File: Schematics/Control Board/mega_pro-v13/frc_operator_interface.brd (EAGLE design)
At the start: 127 x 127 mm, 65 parts, among them J1 AVR_SPI_PRG_6PTH, U1 TLC59282_DBQ_24, U4 FT232RLSSOP, Y1 RESONATORSMD

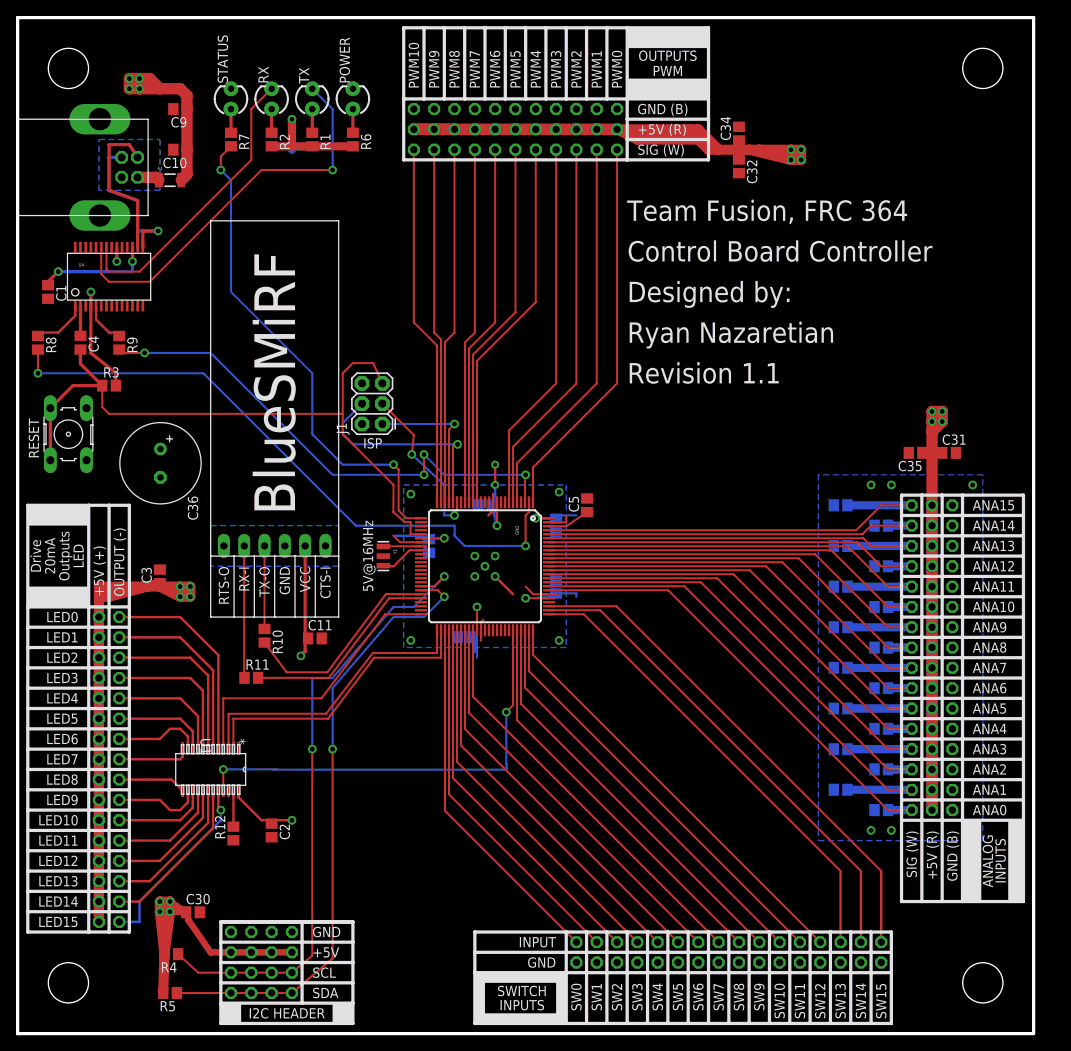
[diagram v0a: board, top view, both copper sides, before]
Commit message: Updated control board schematics and board layout
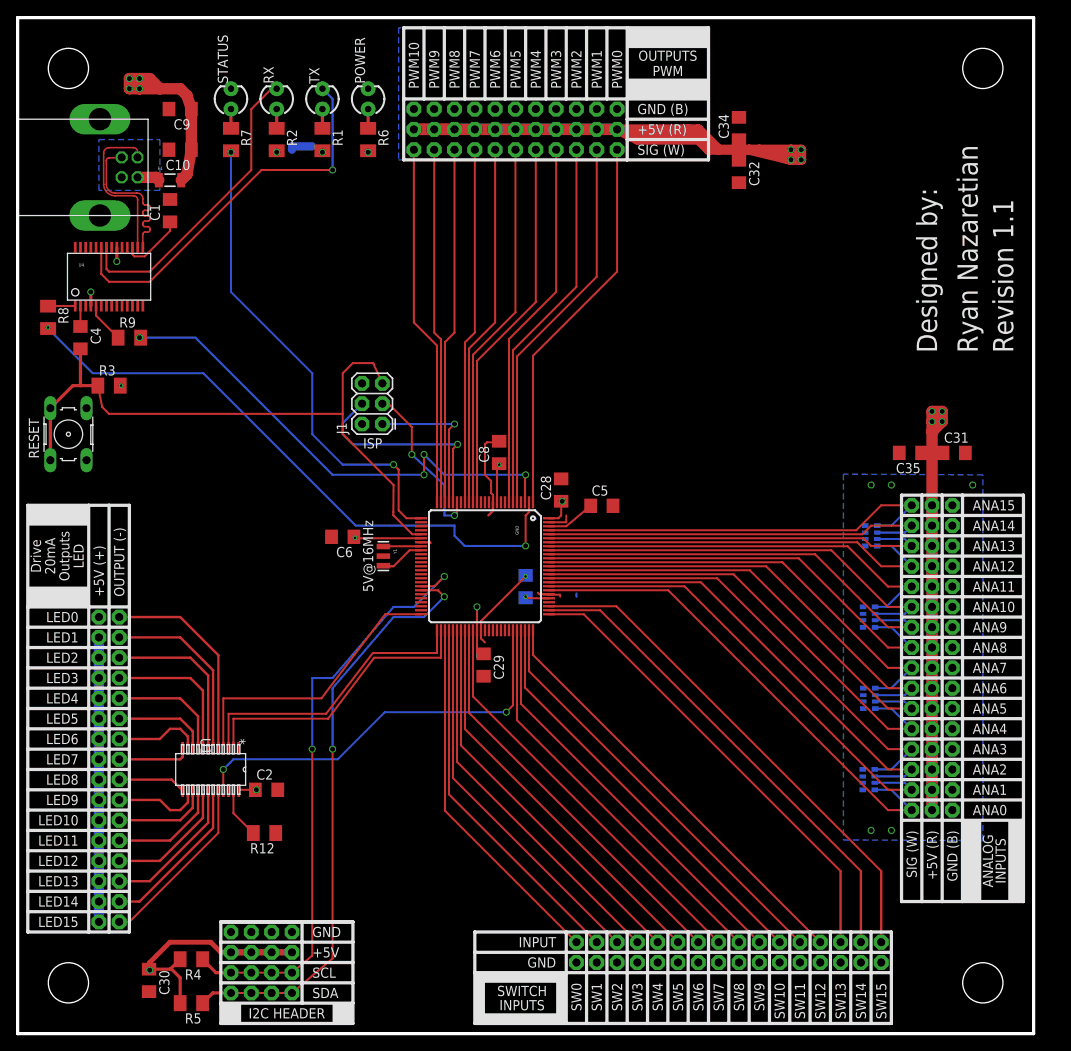
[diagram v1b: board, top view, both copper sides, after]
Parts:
- removed C11, C3: 10uF, resistor:C0805
- removed C12, C13, C14, C15, C16, C17, C18, C19, C20, C21, C22, C23, C24, C25, C26, C27: 1uF, resistor:C0805
- removed C36: 470uF, resistor:E3,5-10
- removed R10, R11: 1K, resistor:R0805
- removed U$19: BLUESMIRF, teamFusion:BLUESMIRF
- added CN1, CN2, CN3, CN4: 1uF, resistor-dil:EXB38V
- C1, C10, C2, C28, C29, C30, C31, C32, C34, C35, C4, C5, C6, C7, C8, C9: device resistor:C0805 -> rcl:C1206
- R1: value 140 -> 280; device resistor:R0805 -> rcl:M1206
- R12, R3, R4, R5, R8, R9: device resistor:R0805 -> rcl:M1206
- R2: value 157.5 -> 315; device resistor:R0805 -> rcl:M1206
- R6: value 85 -> 170; device resistor:R0805 -> rcl:M1206
- R7: value 150 -> 300; device resistor:R0805 -> rcl:M1206
- moved C1 18.3 mm to (19.1, 102.9), turned to 90 degrees
- moved C6 10.9 mm to (40.6, 62.1), flipped to the top, turned to 180 degrees
- moved C30 10.1 mm to (16.4, 6.65), turned to 270 degrees
- moved C8 6.84 mm to (60.2, 72.6), flipped to the top, turned to 90 degrees
- moved C2 5.12 mm to (31.1, 30.5), turned to 0 degrees
- moved C28 4.49 mm to (67.9, 67.9), flipped to the top, turned to 90 degrees
- moved C29 4.19 mm to (58.2, 46.1), flipped to the top, turned to 270 degrees
- moved R12 3.89 mm to (30.9, 25.1), turned to 180 degrees
- moved C7 3.81 mm to (63.5, 55.9)
- moved R8 3.42 mm to (3.81, 89.5)
- moved R5 2.95 mm to (21.7, 3.81)
- moved R4 2.59 mm to (21.7, 9.30)
- moved POWER 1.91 mm to (43.8, 116.8)
- moved R6 1.91 mm to (43.8, 111.8)
- moved C5 1.84 mm to (73.0, 66.0), turned to 0 degrees
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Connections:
- net USB_D+ renamed USB_D_P
- net USB_D- renamed USB_D_N
- removed net N$10: R11.1, U$19.RX-I
- removed net N$9: R10.1, U$19.TX-O
- net 5V: no longer C11.1, C3.1, C36.+, U$19.VCC
- net A0: now also CN4.5; no longer C27.1
- net A1: now also CN4.6; no longer C26.1
- net A10: now also CN2.7; no longer C17.1
- net A11: now also CN2.8; no longer C16.1
- net A12: now also CN1.5; no longer C15.1
- net A13: now also CN1.6; no longer C14.1
- net A14: now also CN1.7; no longer C13.1
- net A15: now also CN1.8; no longer C12.1
- net A2: now also CN4.7; no longer C25.1
- net A3: now also CN4.8; no longer C24.1
- net A4: now also CN3.5; no longer C23.1
- net A5: now also CN3.6; no longer C22.1
- net A6: now also CN3.7; no longer C21.1
- net A7: now also CN3.8; no longer C20.1
- net A8: now also CN2.5; no longer C19.1
- net A9: now also CN2.6; no longer C18.1
- net DIO18(TX1): no longer R11.2
- net DIO19(RX1): no longer R10.2
- net GND: now also CN1.1, CN1.2, CN1.3, CN1.4, CN2.1, CN2.2, CN2.3, CN2.4, CN3.1, CN3.2, CN3.3, CN3.4, CN4.1, CN4.2, CN4.3, CN4.4; no longer C11.2, C12.2, C13.2, C14.2, C15.2, C16.2, C17.2, C18.2, C19.2, C20.2, C21.2, C22.2, C23.2, C24.2, C25.2, C26.2, C27.2, C3.2, C36.-, U$19.GND
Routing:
- net 5V: track 494.3 -> 343.7 mm, vias 32 -> 25
- net DIO19(RX1): track 26.3 -> 0.00 mm
- net DIO18(TX1): track 25.3 -> 0.00 mm
- net N$10: track 16.5 -> 0.00 mm
- net N$9: track 10.4 -> 0.00 mm
- net GND: track 24.0 -> 31.3 mm, vias 19 -> 7
- net N$21: track 14.5 -> 8.12 mm, vias 2 -> 0
- net DIO39: track 55.8 -> 51.6 mm
- net TXD: track 6.92 -> 3.40 mm
- net A2: track 53.8 -> 50.4 mm
- net DIO21(SCL): track 78.8 -> 75.5 mm
- net A10: track 60.5 -> 57.4 mm
- net A6: track 57.2 -> 54.1 mm
- net A14: track 63.9 -> 60.8 mm
- net A15: track 59.7 -> 62.4 mm
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- removed copper zone on layer 16, net N$8
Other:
- board text removed: "Control Board Controller"
- board text removed: "Team Fusion, FRC 364"

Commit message: Final control board revision 1.1
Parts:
- removed C10, C30: 10uF, rcl:C1206
- removed C9: 0.1uF, rcl:C1206
- removed R4, R5: 10k, rcl:M1206
- removed U$15: I2CHEADER, teamFusion:I2CHEADER
- moved R8 57.4 mm to (48.0, 53.0)
- moved R9 52.0 mm to (48.0, 47.6), turned to 270 degrees
- moved CN4 43.8 mm to (71.1, 36.7), flipped to the top
- moved F1 40.6 mm to (18.5, 66.0), turned to 270 degrees
- moved CN3 40.2 mm to (71.2, 32.6), flipped to the top
- moved CN2 37.6 mm to (71.3, 28.6), flipped to the top
- moved U$14 36.8 mm to (0.25, 77.5)
- moved C4 36.6 mm to (34.7, 62.1)
- moved CN1 35.7 mm to (71.4, 24.5), flipped to the top
- moved C7 34.0 mm to (53.8, 23.3), flipped to the top, turned to 270 degrees
- moved C8 33.9 mm to (42.9, 43.4)
- moved GND 33.8 mm to (41.4, 29.2)
- moved J1 33.8 mm to (28.6, 47.0)
- moved POWER 33.8 mm to (26.8, 87.6)
- moved R1 33.8 mm to (21.1, 82.5)
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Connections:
- net 5V: no longer C10.1, C30.1, C9.1, R4.2, R5.2, U$15.VCC@0, U$15.VCC@1, U$15.VCC@2, U$15.VCC@3
- net DIO20(SDA): no longer R5.1, U$15.SDA@0, U$15.SDA@1, U$15.SDA@2, U$15.SDA@3
- net DIO21(SCL): no longer R4.1, U$15.SCL@0, U$15.SCL@1, U$15.SCL@2, U$15.SCL@3
- net GND: no longer C10.2, C30.2, C9.2, U$15.GND@0, U$15.GND@1, U$15.GND@2, U$15.GND@3
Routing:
- net 5V: track 343.7 -> 245.2 mm, vias 25 -> 15
- net DIO21(SCL): track 75.5 -> 0.00 mm, vias 2 -> 0
- net DIO20(SDA): track 74.5 -> 0.00 mm, vias 2 -> 0
- net DIO0(RX0-I): track 77.8 -> 16.6 mm, vias 2 -> 0
- net DIO1(TX0-O): track 62.5 -> 9.64 mm, vias 4 -> 0
- net DIO36: track 46.6 -> 10.7 mm
- net DIO37: track 45.8 -> 9.99 mm
- net DIO35: track 47.5 -> 11.8 mm
- net DIO34: track 48.3 -> 13.7 mm
- net DIO29: track 50.5 -> 16.4 mm
- net DIO33: track 49.2 -> 15.6 mm
- net DIO28: track 51.3 -> 18.3 mm
- net DIO32: track 50.0 -> 17.5 mm
- net DIO24: track 58.6 -> 26.3 mm
- net DIO23: track 61.4 -> 29.3 mm
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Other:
- board size 127 x 127 mm -> 99.1 x 99.1 mm
